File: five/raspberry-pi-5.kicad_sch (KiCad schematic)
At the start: 26 parts, among them J104 Raspberry Pi, SW101 SW_Push, U101 TPM_Infineon_SLB9670

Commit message: Update Library
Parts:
- C101, C102, C103, C105: footprint Capacitor_SMD:C_0603_1608Metric -> V2_Capacitor_SMD:C_0603; symbol Device:C_Small -> V2_Capacitor:0603_0u1; Manufacturer (none) -> TDK; Mouser (none) -> 810-CGA3E2X7R1H104MA; Product (none) -> CGA3E2X7R1H104M080AA; Rating (none) -> 50V
- C104: footprint Capacitor_SMD:C_0603_1608Metric -> V2_Capacitor_SMD:C_0603; symbol Device:C_Small -> V2_Capacitor:0603_10u; Manufacturer (none) -> TDK; Mouser (none) -> 810-C1608X6S1A106M; Product (none) -> C1608X6S1A106M080AC; Rating (none) -> 10V
- D101, D102: footprint LED_SMD:LED_0603_1608Metric -> V2_LED:LED_0603; symbol Device:LED_Small -> V2_LED:0603_Orange; Manufacturer (none) -> ROHM Semiconductor; Mouser (none) -> 755-SML-D12D1WT86; Product (none) -> SML-D12D1WT86
- FID101, FID102, FID103: value Fiducial -> Fiducial_Paste
- H101, H102, H103, H104: value MountingHole_2.5mm_PadTop_5mm -> 2.5mm_PadTop_5mm
- INFO101: value ORDER-NUMBER -> ~; footprint V2_Production:Order_Number -> V2_Production:Revision; symbol V2_Production:Order_Number -> V2_Production:Revision
- J104: value Raspberry Pi -> ~
- R103, R104: footprint Resistor_SMD:R_0603_1608Metric -> V2_Resistor_SMD:R_0603; symbol Device:R_Small -> V2_Resistor:0603_330R; Manufacturer (none) -> Vishay; Mouser (none) -> 71-CRCW0603330RFKEAC; Product (none) -> CRCW0603330RFKEAC; Rating (none) -> 100mW
- R105: value 5K1 -> 5k1; footprint Resistor_SMD:R_0603_1608Metric -> V2_Resistor_SMD:R_0603; symbol Device:R_Small -> V2_Resistor:0603_5k1; Manufacturer (none) -> Vishay; Mouser (none) -> 71-CRCW06035K10FKEAC; Product (none) -> CRCW06035K10FKEAC; Rating (none) -> 100mW
- R106: footprint Resistor_SMD:R_0603_1608Metric -> V2_Resistor_SMD:R_0603; symbol Device:R_Small -> V2_Resistor:0603_10k; Manufacturer (none) -> Vishay; Mouser (none) -> 71-CRCW060310K0FKEAC; Product (none) -> CRCW060310K0FKEAC; Rating (none) -> 100mW
- SW101: value SW_Push -> SKSG; symbol Switch:SW_Push -> V2_Switch:SKSG; Manufacturer (none) -> Alps Alpine; Mouser (none) -> 688-SKSGACE010; Product (none) -> SKSGACE010
- renumbered H105 to RP105
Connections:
- net +3.3V renamed +3V3

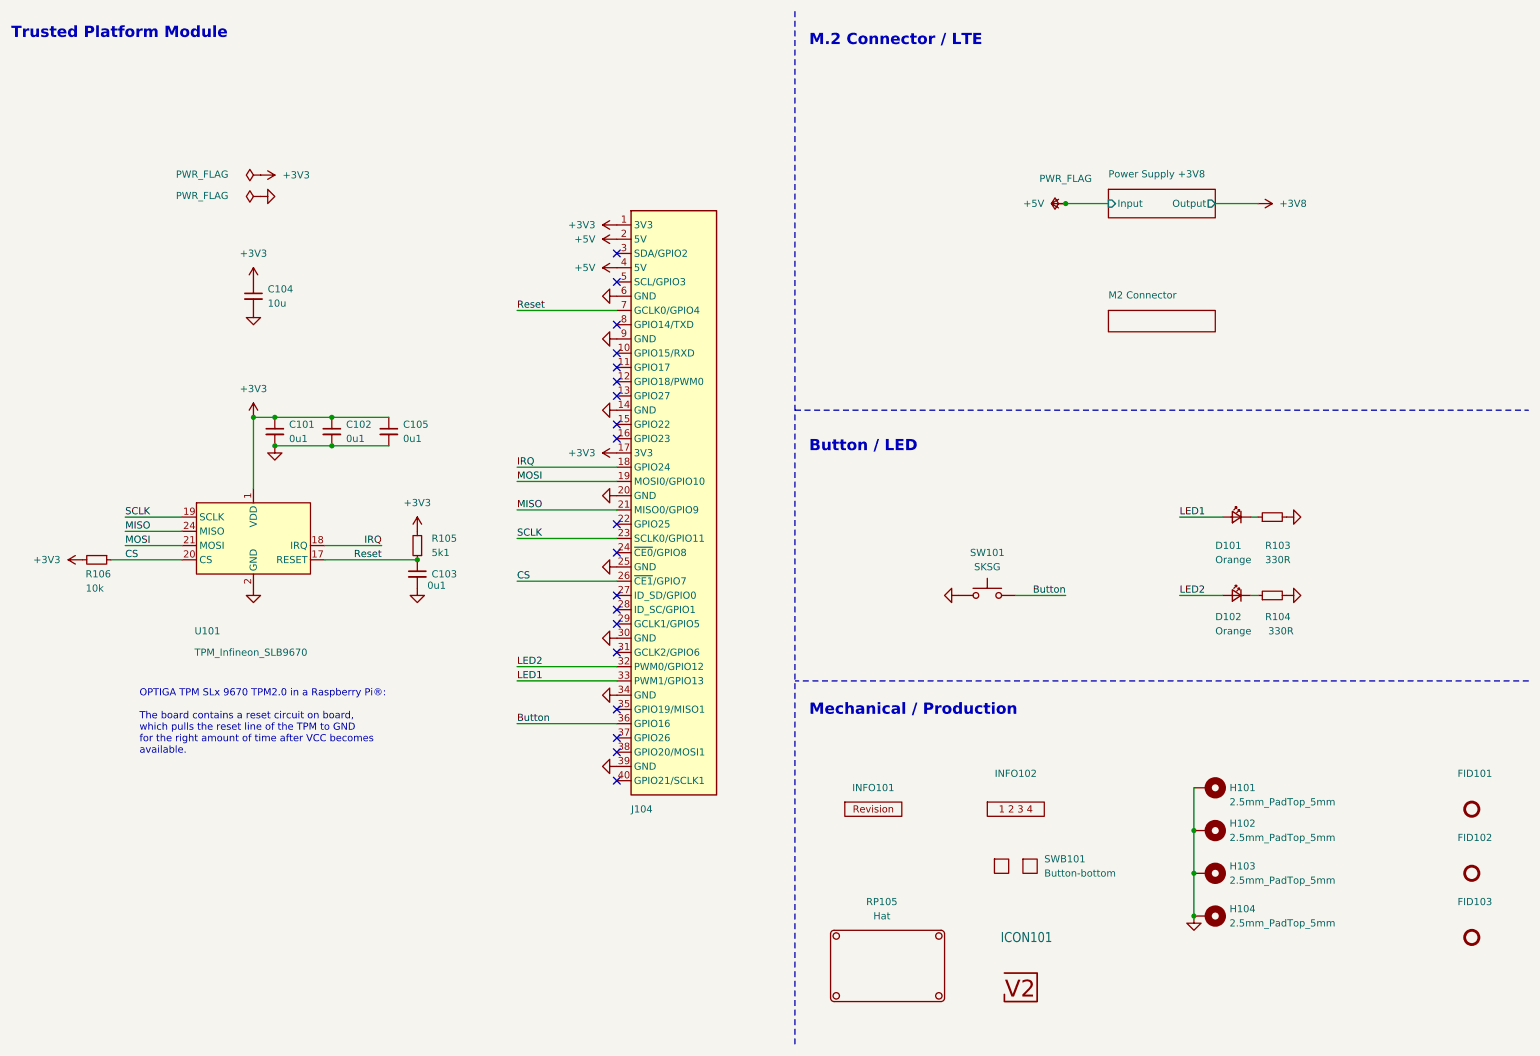
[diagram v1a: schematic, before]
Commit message: KiCad 10
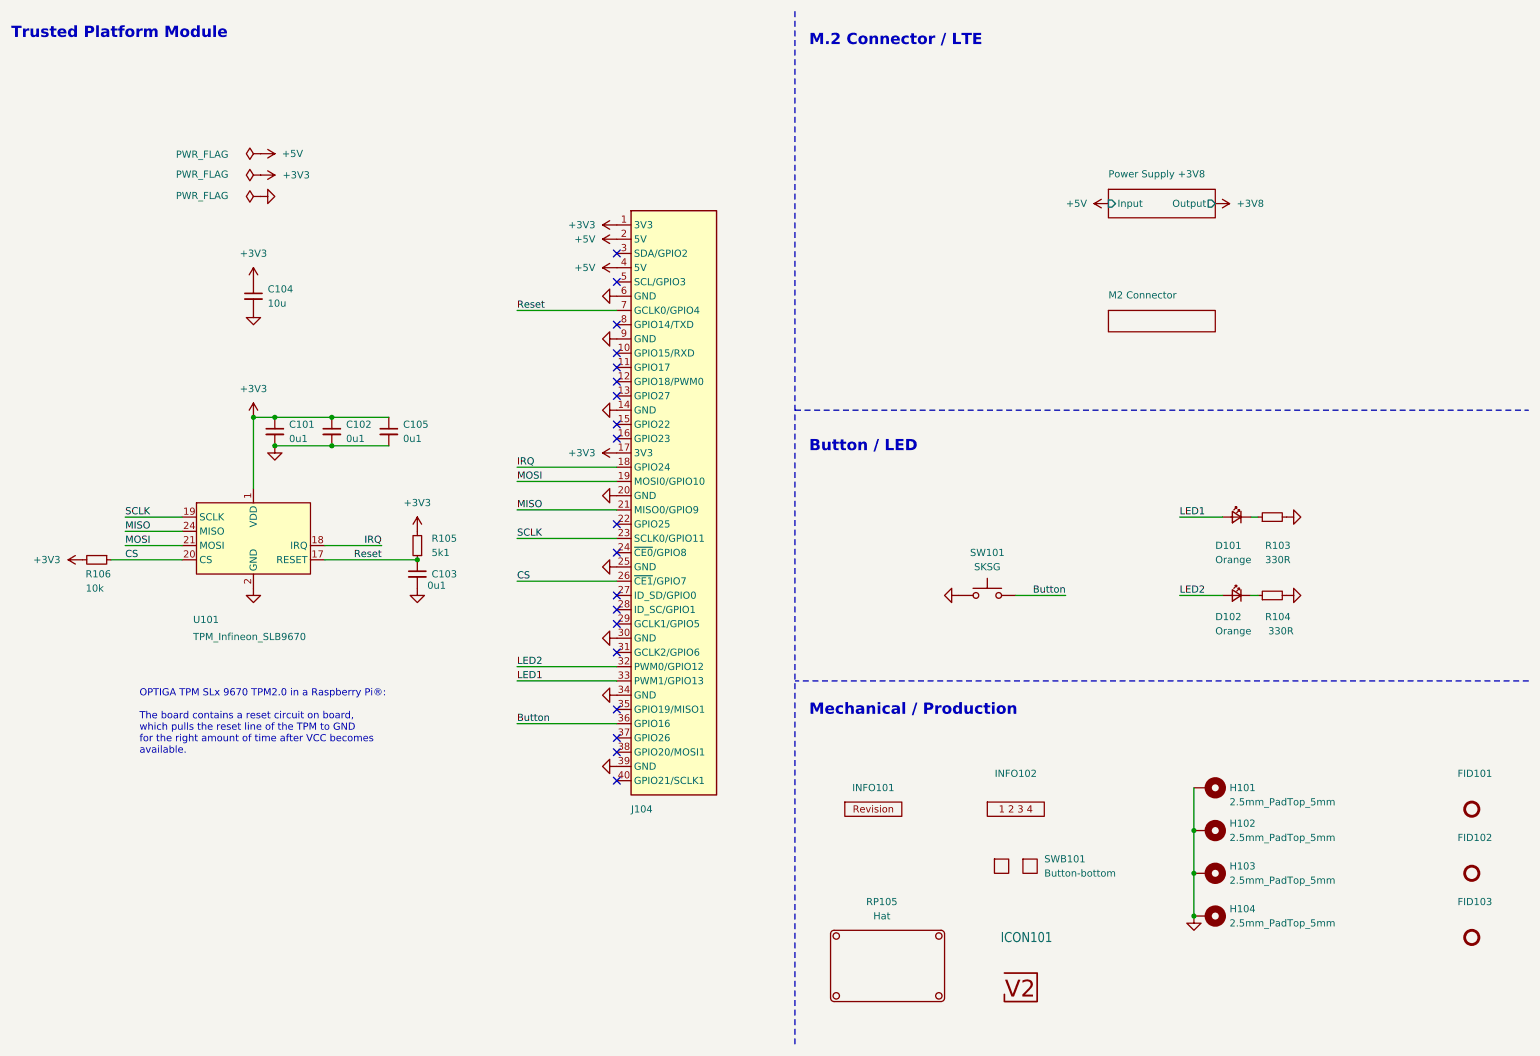
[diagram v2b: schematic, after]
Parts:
- INFO101, J104: value ~ -> (none)
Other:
- company: WebThing -> Trusted Platform Module

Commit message: Replace step-down
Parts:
- SW101: Rating (none) -> 1.6N
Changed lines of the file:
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@@
 	(title_block
 		(title "Raspberry Pi 5")
-		(date "2026-02-15")
-		(rev "2026-02-15")
+		(date "2026-03-31")
+		(rev "2026-03-31")
 		(company "Trusted Platform Module")
 	)
@@
 			)
 		)
+		(property "Sim.Enable" "0"
+			(at 170.18 182.88 0)
+			(hide yes)
+			(show_name no)
+			(do_not_autoplace no)
+			(effects
+				(font
+					(size 1.27 1.27)
+				)
+			)
+		)
 		(instances
 			(project "raspberry-pi-5"
@@
 			)
 		)
+		(property "Rating" "1.6N"
+			(at 187.96 137.16 0)
+			(hide yes)
+			(show_name no)
+			(do_not_autoplace no)
+			(effects
+				(font
+					(size 1.27 1.27)
+				)
+			)
+		)
 		(pin "1"
 		)
@@
 		(in_pos_files yes)
 		(dnp no)
-		(property "Reference" "#FLG0101"
+		(property "Reference" "#FLG101"
 			(at 58.42 36.195 0)
 			(hide yes)
@@
 			(project "raspberry-pi-5"
 				(path "/6c8448b4-b04d-47e1-934e-e40cbe27a7be"
-					(reference "#FLG0101")
+					(reference "#FLG101")
 					(unit 1)
 				)
@@
 		(dnp no)
 		(fields_autoplaced yes)
-		(property "Reference" "#PWR0130"
+		(property "Reference" "#PWR130"
 			(at 213.36 46.99 0)
 			(hide yes)
@@
 			(project "raspberry-pi-5"
 				(path "/6c8448b4-b04d-47e1-934e-e40cbe27a7be"
-					(reference "#PWR0130")
+					(reference "#PWR130")
 					(unit 1)
 				)
@@
 		(dnp no)
 		(fields_autoplaced yes)
-		(property "Reference" "#PWR0132"
+		(property "Reference" "#PWR132"
 			(at 54.61 38.1 0)
 			(hide yes)
@@
 			(project "raspberry-pi-5"
 				(path "/6c8448b4-b04d-47e1-934e-e40cbe27a7be"
-					(reference "#PWR0132")
+					(reference "#PWR132")
 					(unit 1)
 				)
@@
 			)
 		)
+		(property "Sim.Enable" "0"
+			(at 193.04 165.1 0)
+			(hide yes)
+			(show_name no)
+			(do_not_autoplace no)
+			(effects
+				(font
+					(size 1.27 1.27)
+				)
+			)
+		)
 		(instances
 			(project "raspberry-pi-5"
@@
 			(at 132.08 99.06 0)
 			(hide yes)
+			(show_name no)
+			(do_not_autoplace no)
+			(effects
+				(font
+					(size 1.27 1.27)
+				)
+			)
+		)
+		(property "Sim.Enable" "0"
+			(at 132.08 99.06 0)
+			(hide yes)

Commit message: Good Bye Imperial
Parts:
- C101, C102, C103, C105: footprint V2_Capacitor_SMD:C_0603 -> V2_Capacitor_SMD:C_1608; symbol V2_Capacitor:0603_0u1 -> V2_Capacitor:1608_0u1
- C104: footprint V2_Capacitor_SMD:C_0603 -> V2_Capacitor_SMD:C_1608; symbol V2_Capacitor:0603_10u -> V2_Capacitor:1608_10u
- D101, D102: symbol V2_LED:0603_Orange -> V2_LED:1608_Orange
- R103, R104: footprint V2_Resistor_SMD:R_0603 -> V2_Resistor_SMD:R_1608; symbol V2_Resistor:0603_330R -> V2_Resistor:1608_330R
- R105: footprint V2_Resistor_SMD:R_0603 -> V2_Resistor_SMD:R_1608; symbol V2_Resistor:0603_5k1 -> V2_Resistor:1608_5k1
- R106: footprint V2_Resistor_SMD:R_0603 -> V2_Resistor_SMD:R_1608; symbol V2_Resistor:0603_10k -> V2_Resistor:1608_10k
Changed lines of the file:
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@@
 	)
 	(symbol
-		(lib_id "V2_LED:0603_Orange")
+		(lib_id "V2_LED:1608_Orange")
 		(at 232.41 116.84 0)
 		(mirror y)
@@
 	)
 	(symbol
-		(lib_id "V2_Resistor:0603_5k1")
+		(lib_id "V2_Resistor:1608_5k1")
 		(at 86.36 107.95 180)
 		(unit 1)
@@
 			)
 		)
-		(property "Footprint" "V2_Resistor_SMD:R_0603"
+		(property "Footprint" "V2_Resistor_SMD:R_1608"
 			(at 86.36 92.202 0)
 			(hide yes)
@@
 	)
 	(symbol
-		(lib_id "V2_Resistor:0603_330R")
+		(lib_id "V2_Resistor:1608_330R")
 		(at 238.76 102.87 90)
 		(unit 1)
@@
 			)
 		)
-		(property "Footprint" "V2_Resistor_SMD:R_0603"
+		(property "Footprint" "V2_Resistor_SMD:R_1608"
 			(at 254.508 102.87 0)
 			(hide yes)
@@
 	)
 	(symbol
-		(lib_id "V2_LED:0603_Orange")
+		(lib_id "V2_LED:1608_Orange")
 		(at 232.41 102.87 0)
 		(mirror y)
@@
 	)
 	(symbol
-		(lib_id "V2_Capacitor:0603_0u1")
+		(lib_id "V2_Capacitor:1608_0u1")
 		(at 60.96 87.63 0)
 		(unit 1)
@@
 			)
 		)
-		(property "Footprint" "V2_Capacitor_SMD:C_0603"
+		(property "Footprint" "V2_Capacitor_SMD:C_1608"
 			(at 60.96 104.648 0)
 			(hide yes)
@@
 	)
 	(symbol
-		(lib_id "V2_Capacitor:0603_0u1")
+		(lib_id "V2_Capacitor:1608_0u1")
 		(at 81.28 87.63 0)
 		(unit 1)
@@
 			)
 		)
-		(property "Footprint" "V2_Capacitor_SMD:C_0603"
+		(property "Footprint" "V2_Capacitor_SMD:C_1608"
 			(at 81.28 104.648 0)
 			(hide yes)
@@
 	)
 	(symbol
-		(lib_id "V2_Resistor:0603_10k")
+		(lib_id "V2_Resistor:1608_10k")
 		(at 29.21 110.49 270)
 		(unit 1)
@@
 			)
 		)
-		(property "Footprint" "V2_Resistor_SMD:R_0603"
+		(property "Footprint" "V2_Resistor_SMD:R_1608"
 			(at 13.462 110.49 0)
 			(hide yes)
@@
 	)
 	(symbol
-		(lib_id "V2_Capacitor:0603_10u")
+		(lib_id "V2_Capacitor:1608_10u")
 		(at 57.15 63.5 0)
 		(unit 1)
@@
 			)
 		)
-		(property "Footprint" "V2_Capacitor_SMD:C_0603"
+		(property "Footprint" "V2_Capacitor_SMD:C_1608"
 			(at 57.15 80.518 0)
 			(hide yes)
@@
 	)
 	(symbol
-		(lib_id "V2_Capacitor:0603_0u1")
+		(lib_id "V2_Capacitor:1608_0u1")
 		(at 86.36 113.03 0)
 		(unit 1)
@@
 			)
 		)
-		(property "Footprint" "V2_Capacitor_SMD:C_0603"
+		(property "Footprint" "V2_Capacitor_SMD:C_1608"
 			(at 86.36 130.048 0)
 			(hide yes)
@@
 	)
 	(symbol
-		(lib_id "V2_Capacitor:0603_0u1")
+		(lib_id "V2_Capacitor:1608_0u1")
 		(at 71.12 87.63 0)
 		(unit 1)
@@
 			)
 		)
-		(property "Footprint" "V2_Capacitor_SMD:C_0603"
+		(property "Footprint" "V2_Capacitor_SMD:C_1608"
 			(at 71.12 104.648 0)
 			(hide yes)
@@
 	)
 	(symbol
-		(lib_id "V2_Resistor:0603_330R")
+		(lib_id "V2_Resistor:1608_330R")
 		(at 238.76 116.84 90)
 		(unit 1)
@@
 			)
 		)
-		(property "Footprint" "V2_Resistor_SMD:R_0603"
+		(property "Footprint" "V2_Resistor_SMD:R_1608"
 			(at 254.508 116.84 0)
 			(hide yes)
